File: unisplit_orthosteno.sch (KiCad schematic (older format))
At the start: 53 parts, among them U1 ProMicro

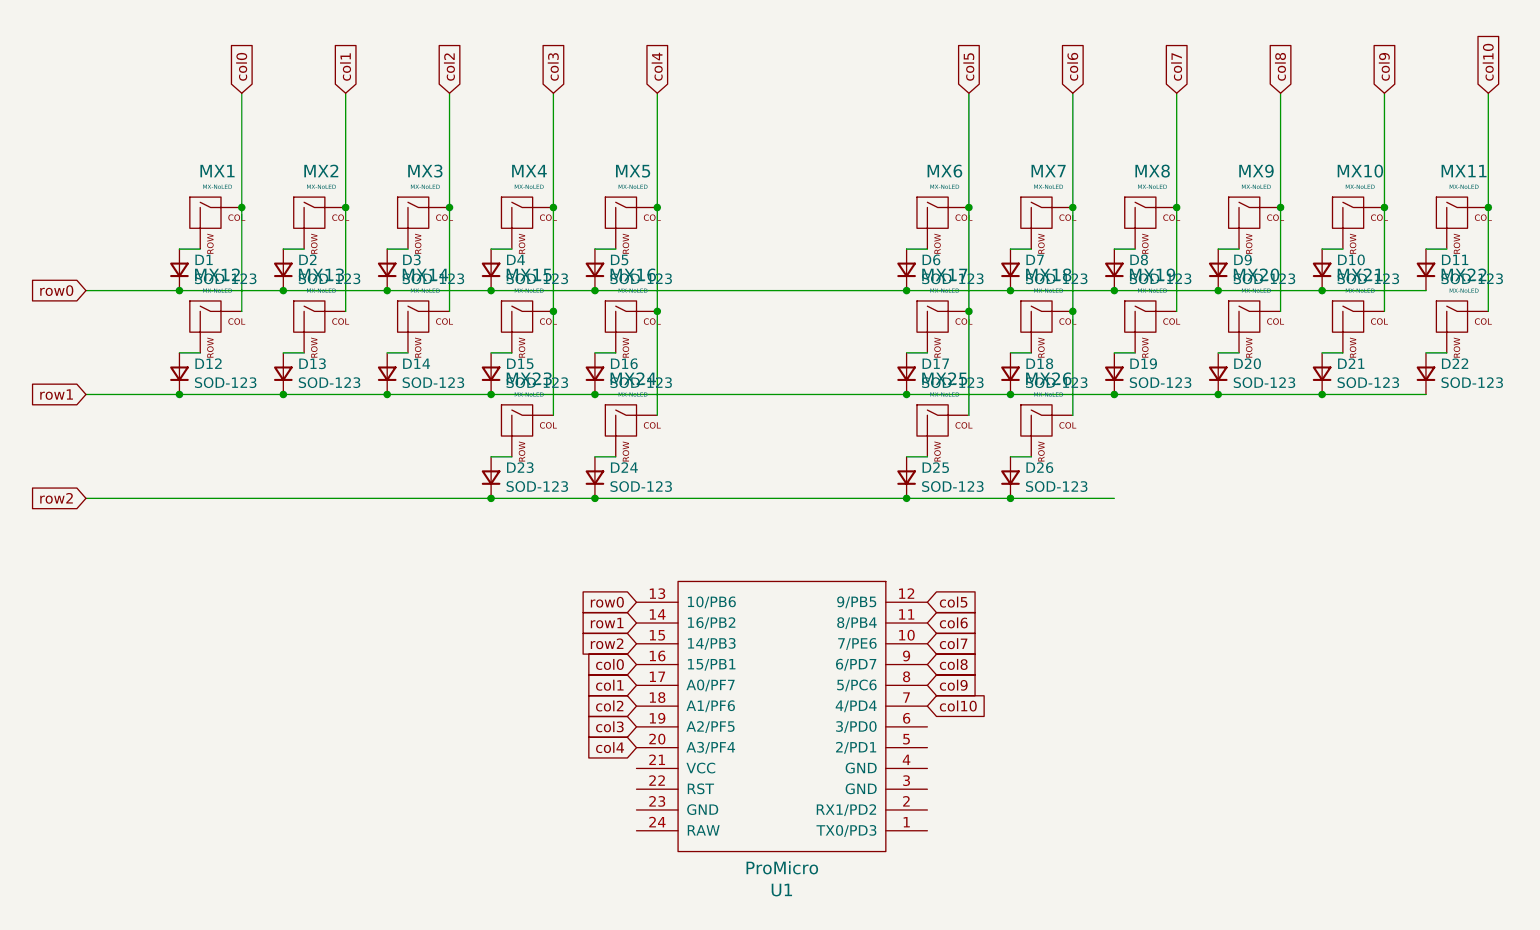
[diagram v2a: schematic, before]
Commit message: finished routing but possible problem in column 3 and 4 which I asked and reddit
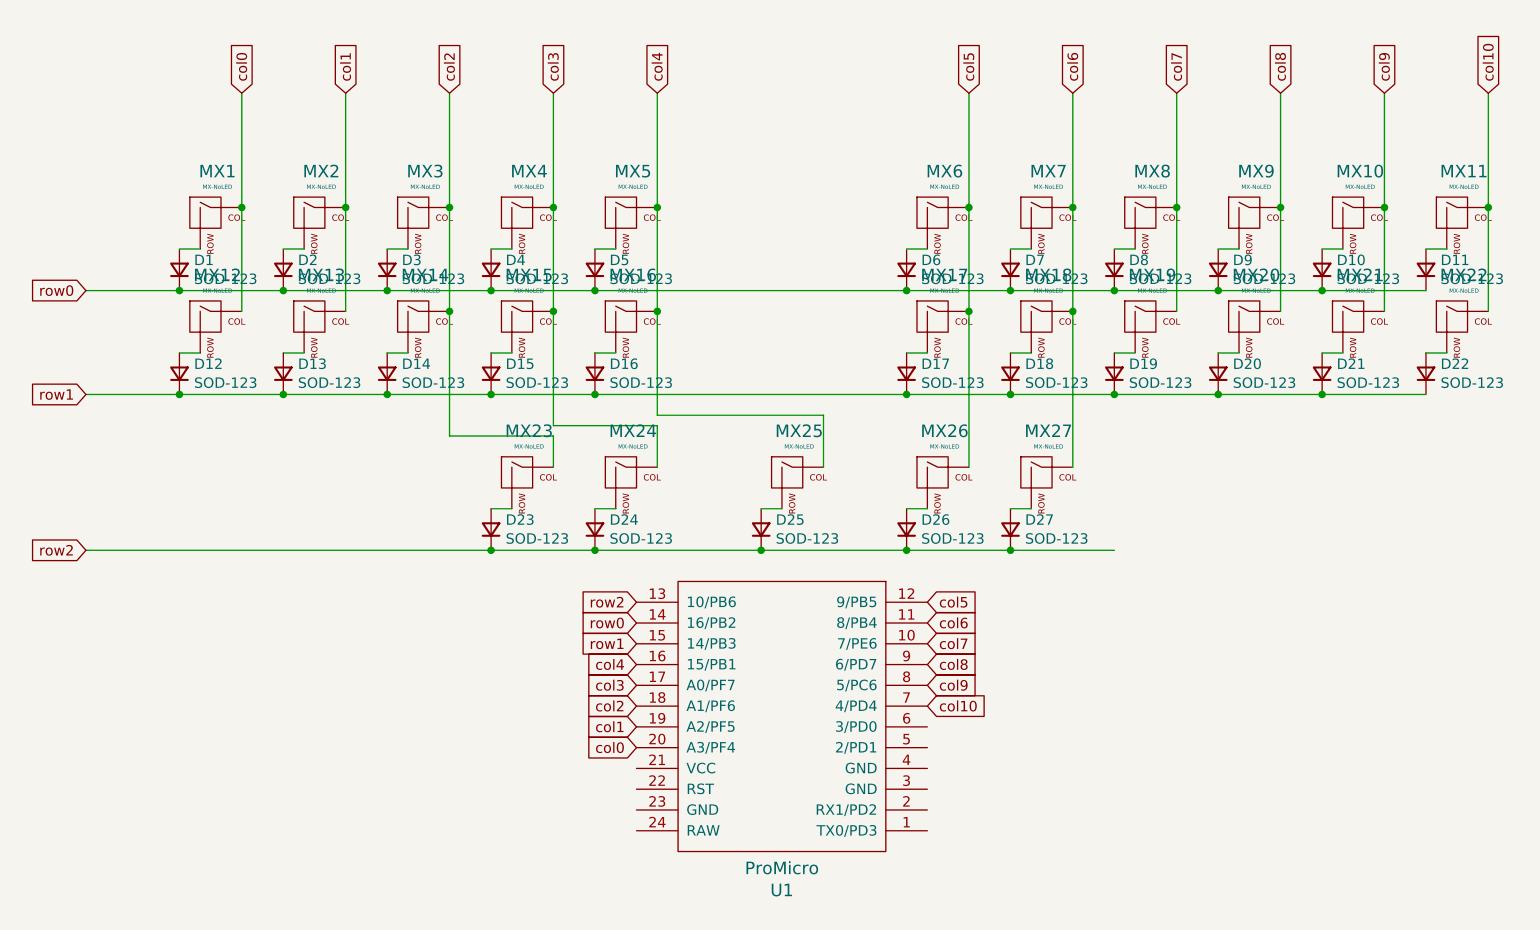
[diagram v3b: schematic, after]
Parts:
- added D25: SOD-123, Keebio-Parts:D_SOD123, symbol Device:D_Small
- added MX25: MX-NoLED, Keebio-Parts:MX-Alps-Choc-1U-NoLED, symbol MX_Alps_Hybrid:MX-NoLED
- renumbered D25 to D26, D26 to D27, MX25 to MX26, MX26 to MX27
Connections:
- net col0: now also U1.20 (A3/PF4); no longer U1.16 (15/PB1)
- net col1: now also U1.19 (A2/PF5); no longer U1.17 (A0/PF7)
- net col2: now also MX23.1 (COL)
- net col3: now also MX24.1 (COL), U1.17 (A0/PF7); no longer MX23.1 (COL), U1.19 (A2/PF5)
- net col4: now also U1.16 (15/PB1), MX25.1 (COL); no longer MX24.1 (COL), U1.20 (A3/PF4)
- net row0: now also U1.14 (16/PB2); no longer U1.13 (10/PB6)
- net row1: now also U1.15 (14/PB3); no longer U1.14 (16/PB2)
- net row2: now also U1.13 (10/PB6), D25.1 (K); no longer U1.15 (14/PB3)
- new net: D25.2 (A), MX25.2 (ROW)
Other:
- moved on the sheet: D23, D24, D26, D27, MX23, MX24, MX26, MX27
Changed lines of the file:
@@
-$Comp
-L MX_Alps_Hybrid:MX-NoLED MX?
-U 1 1 6009990C
-P 4100 3100
-AR Path="/6008E628" Ref="MX?"  Part="1"
-AR Path="/6009990C" Ref="MX23"  Part="1"
-F 0 "MX23" H 4133 3323 60  0000 C CNN
-F 1 "MX-NoLED" H 4133 3249 20  0000 C CNN
-F 2 "Keebio-Parts:MX-Alps-Choc-1U-NoLED" H 3475 3075 60  0001 C CNN
-F 3 "" H 3475 3075 60  0001 C CNN
-	1    4100 3100
-	1    0    0    -1
-$EndComp
-$Comp
-L MX_Alps_Hybrid:MX-NoLED MX24
-U 1 1 600999EE
-P 4600 3100
-F 0 "MX24" H 4633 3323 60  0000 C CNN
-F 1 "MX-NoLED" H 4633 3249 20  0000 C CNN
-F 2 "Keebio-Parts:MX-Alps-Choc-1U-NoLED" H 3975 3075 60  0001 C CNN
-F 3 "" H 3975 3075 60  0001 C CNN
-	1    4600 3100
-	1    0    0    -1
-$EndComp
 $Comp
 L MX_Alps_Hybrid:MX-NoLED MX?
@@
 $Comp
 L MX_Alps_Hybrid:MX-NoLED MX?
-U 1 1 6009A7CA
-P 6100 3100
-AR Path="/6008E628" Ref="MX?"  Part="1"
-AR Path="/6009A7CA" Ref="MX25"  Part="1"
-F 0 "MX25" H 6133 3323 60  0000 C CNN
-F 1 "MX-NoLED" H 6133 3249 20  0000 C CNN
-F 2 "Keebio-Parts:MX-Alps-Choc-1U-NoLED" H 5475 3075 60  0001 C CNN
-F 3 "" H 5475 3075 60  0001 C CNN
-	1    6100 3100
-	1    0    0    -1
-$EndComp
-$Comp
-L MX_Alps_Hybrid:MX-NoLED MX26
-U 1 1 6009A7D4
-P 6600 3100
-F 0 "MX26" H 6633 3323 60  0000 C CNN
-F 1 "MX-NoLED" H 6633 3249 20  0000 C CNN
-F 2 "Keebio-Parts:MX-Alps-Choc-1U-NoLED" H 5975 3075 60  0001 C CNN
-F 3 "" H 5975 3075 60  0001 C CNN
-	1    6600 3100
-	1    0    0    -1
-$EndComp
-$Comp
-L MX_Alps_Hybrid:MX-NoLED MX?
 U 1 1 600A326C
 P 8600 2100
@@
 	0    -1   -1   0
 $EndComp
-$Comp
-L Device:D_Small D23
-U 1 1 600BD975
-P 3950 3350
-F 0 "D23" V 3996 3280 50  0000 R CNN
-F 1 "SOD-123" V 3905 3280 50  0000 R CNN
-F 2 "Keebio-Parts:D_SOD123" V 3950 3350 50  0001 C CNN
-F 3 "~" V 3950 3350 50  0001 C CNN
-	1    3950 3350
-	0    -1   -1   0
-$EndComp
-$Comp
-L Device:D_Small D24
-U 1 1 600BE1C4
-P 4450 3350
-F 0 "D24" V 4496 3280 50  0000 R CNN
-F 1 "SOD-123" V 4405 3280 50  0000 R CNN
-F 2 "Keebio-Parts:D_SOD123" V 4450 3350 50  0001 C CNN
-F 3 "~" V 4450 3350 50  0001 C CNN
-	1    4450 3350
-	0    -1   -1   0
-$EndComp
-$Comp
-L Device:D_Small D25
-U 1 1 600BE3C9
-P 5950 3350
-F 0 "D25" V 5996 3280 50  0000 R CNN
-F 1 "SOD-123" V 5905 3280 50  0000 R CNN
-F 2 "Keebio-Parts:D_SOD123" V 5950 3350 50  0001 C CNN
-F 3 "~" V 5950 3350 50  0001 C CNN
-	1    5950 3350
-	0    -1   -1   0
-$EndComp
-$Comp
-L Device:D_Small D26
-U 1 1 600BE81C
-P 6450 3350
-F 0 "D26" V 6496 3280 50  0000 R CNN
-F 1 "SOD-123" V 6405 3280 50  0000 R CNN
-F 2 "Keebio-Parts:D_SOD123" V 6450 3350 50  0001 C CNN
-F 3 "~" V 6450 3350 50  0001 C CNN
-	1    6450 3350
-	0    -1   -1   0
-$EndComp
 Wire Wire Line
 	2450 2250 2550 2250
@@
 	4450 2750 4550 2750
 Wire Wire Line
-	3950 3250 4050 3250
-Wire Wire Line
-	4450 3250 4550 3250
-Wire Wire Line
 	5950 2250 6050 2250
 Wire Wire Line
@@
 Wire Wire Line
 	5950 2750 6050 2750
-Wire Wire Line
-	5950 3250 6050 3250
-Wire Wire Line
-	6450 3250 6550 3250
 Wire Wire Line
 	7450 2250 7550 2250
@@
 Wire Wire Line
 	7950 2950 8450 2950
-Wire Wire Line
-	6950 3450 6450 3450
-Connection ~ 3950 3450
-Connection ~ 6450 3450
-Wire Wire Line
-	6450 3450 5950 3450
 Wire Wire Line
 	2750 2550 2750 2050
@@
 Text GLabel 2000 2950 0    50   Input ~ 0
 row1
-Text GLabel 2000 3450 0    50   Input ~ 0
-row2
 Text GLabel 2750 1500 1    50   Input ~ 0
 col0
@@
 	-1   0    0    1
 $EndComp
+Text GLabel 4650 4050 0    50   Input ~ 0
+row0
+Text GLabel 4650 4150 0    50   Input ~ 0
+row1
 Text GLabel 4650 3950 0    50   Input ~ 0
-row0
-Text GLabel 4650 4050 0    50   Input ~ 0
-row1
-Text GLabel 4650 4150 0    50   Input ~ 0
 row2
-Text GLabel 4650 4250 0    50   Input ~ 0
+Text GLabel 4650 4650 0    50   Input ~ 0
 col0
-Text GLabel 4650 4350 0    50   Input ~ 0
+Text GLabel 4650 4550 0    50   Input ~ 0
 col1
 Text GLabel 4650 4450 0    50   Input ~ 0
 col2
-Text GLabel 4650 4550 0    50   Input ~ 0
-col3
-Text GLabel 4650 4650 0    50   Input ~ 0
-col4
 Text GLabel 6050 3950 2    50   Input ~ 0
 col5
@@
 Text GLabel 6050 4450 2    50   Input ~ 0
 col10
-Connection ~ 4450 3450
-Wire Wire Line
-	4450 3450 3950 3450
-Wire Wire Line
-	2000 3450 3950 3450
-Connection ~ 5950 3450
-Wire Wire Line
-	5950 3450 4450 3450
-Wire Wire Line
-	4250 2550 4250 3050
+$Comp
+L MX_Alps_Hybrid:MX-NoLED MX?
+U 1 1 6009990C
+P 4100 3350
+AR Path="/6008E628" Ref="MX?"  Part="1"
+AR Path="/6009990C" Ref="MX23"  Part="1"
+F 0 "MX23" H 4133 3573 60  0000 C CNN
+F 1 "MX-NoLED" H 4133 3499 20  0000 C CNN
+F 2 "Keebio-Parts:MX-Alps-Choc-1U-NoLED" H 3475 3325 60  0001 C CNN
+F 3 "" H 3475 3325 60  0001 C CNN
+	1    4100 3350
+	1    0    0    -1
+$EndComp
+$Comp
+L MX_Alps_Hybrid:MX-NoLED MX24
+U 1 1 600999EE
+P 4600 3350
+F 0 "MX24" H 4633 3573 60  0000 C CNN
+F 1 "MX-NoLED" H 4633 3499 20  0000 C CNN
+F 2 "Keebio-Parts:MX-Alps-Choc-1U-NoLED" H 3975 3325 60  0001 C CNN
+F 3 "" H 3975 3325 60  0001 C CNN
+	1    4600 3350
+	1    0    0    -1
+$EndComp
+$Comp
+L MX_Alps_Hybrid:MX-NoLED MX?
+U 1 1 6009A7CA
+P 6100 3350
+AR Path="/6008E628" Ref="MX?"  Part="1"
+AR Path="/6009A7CA" Ref="MX26"  Part="1"
+F 0 "MX26" H 6133 3573 60  0000 C CNN
+F 1 "MX-NoLED" H 6133 3499 20  0000 C CNN
+F 2 "Keebio-Parts:MX-Alps-Choc-1U-NoLED" H 5475 3325 60  0001 C CNN
+F 3 "" H 5475 3325 60  0001 C CNN
+	1    6100 3350
+	1    0    0    -1
+$EndComp
+$Comp
+L MX_Alps_Hybrid:MX-NoLED MX27
+U 1 1 6009A7D4
+P 6600 3350
+F 0 "MX27" H 6633 3573 60  0000 C CNN
+F 1 "MX-NoLED" H 6633 3499 20  0000 C CNN
+F 2 "Keebio-Parts:MX-Alps-Choc-1U-NoLED" H 5975 3325 60  0001 C CNN
+F 3 "" H 5975 3325 60  0001 C CNN
+	1    6600 3350
+	1    0    0    -1
+$EndComp
+$Comp
+L Device:D_Small D23
+U 1 1 600BD975
+P 3950 3600
+F 0 "D23" V 3996 3530 50  0000 R CNN
+F 1 "SOD-123" V 3905 3530 50  0000 R CNN
+F 2 "Keebio-Parts:D_SOD123" V 3950 3600 50  0001 C CNN
+F 3 "~" V 3950 3600 50  0001 C CNN
+	1    3950 3600
+	0    -1   -1   0
+$EndComp
+$Comp
+L Device:D_Small D24
+U 1 1 600BE1C4
+P 4450 3600
+F 0 "D24" V 4496 3530 50  0000 R CNN
+F 1 "SOD-123" V 4405 3530 50  0000 R CNN
+F 2 "Keebio-Parts:D_SOD123" V 4450 3600 50  0001 C CNN
+F 3 "~" V 4450 3600 50  0001 C CNN
+	1    4450 3600
+	0    -1   -1   0
+$EndComp
+$Comp
+L Device:D_Small D26
+U 1 1 600BE3C9
+P 5950 3600
+F 0 "D26" V 5996 3530 50  0000 R CNN
+F 1 "SOD-123" V 5905 3530 50  0000 R CNN
+F 2 "Keebio-Parts:D_SOD123" V 5950 3600 50  0001 C CNN
+F 3 "~" V 5950 3600 50  0001 C CNN
+	1    5950 3600
+	0    -1   -1   0
+$EndComp
+$Comp
+L Device:D_Small D27
+U 1 1 600BE81C
+P 6450 3600
+F 0 "D27" V 6496 3530 50  0000 R CNN
+F 1 "SOD-123" V 6405 3530 50  0000 R CNN
+F 2 "Keebio-Parts:D_SOD123" V 6450 3600 50  0001 C CNN
+F 3 "~" V 6450 3600 50  0001 C CNN
+	1    6450 3600
+	0    -1   -1   0
+$EndComp
+Wire Wire Line
+	3950 3500 4050 3500
+Wire Wire Line
+	4450 3500 4550 3500
+Wire Wire Line
+	5950 3500 6050 3500
+Wire Wire Line
+	6450 3500 6550 3500
+Wire Wire Line
+	6950 3700 6450 3700
+Connection ~ 3950 3700
+Connection ~ 6450 3700
+Wire Wire Line
+	6450 3700 5950 3700
+Text GLabel 2000 3700 0    50   Input ~ 0
+row2
+Connection ~ 4450 3700
+Wire Wire Line
+	4450 3700 3950 3700
+Wire Wire Line
+	2000 3700 3950 3700
+Connection ~ 5950 3700
+Wire Wire Line
+	5950 3700 5250 3700
+$Comp
+L MX_Alps_Hybrid:MX-NoLED MX?
+U 1 1 600EED95
+P 5400 3350
+AR Path="/6008E628" Ref="MX?"  Part="1"
+AR Path="/600EED95" Ref="MX25"  Part="1"
+F 0 "MX25" H 5433 3573 60  0000 C CNN
+F 1 "MX-NoLED" H 5433 3499 20  0000 C CNN
+F 2 "Keebio-Parts:MX-Alps-Choc-1U-NoLED" H 4775 3325 60  0001 C CNN
+F 3 "" H 4775 3325 60  0001 C CNN
+	1    5400 3350
+	1    0    0    -1
+$EndComp
+$Comp
+L Device:D_Small D25
+U 1 1 600EF1FB
+P 5250 3600
+F 0 "D25" V 5296 3530 50  0000 R CNN
+F 1 "SOD-123" V 5205 3530 50  0000 R CNN
+F 2 "Keebio-Parts:D_SOD123" V 5250 3600 50  0001 C CNN
+F 3 "~" V 5250 3600 50  0001 C CNN
+	1    5250 3600
+	0    -1   -1   0
+$EndComp
+Wire Wire Line
+	5250 3500 5350 3500
+Connection ~ 5250 3700
+Wire Wire Line
+	5250 3700 4450 3700
+Wire Wire Line
+	6250 3300 6250 2550
+Connection ~ 6250 2550
+Wire Wire Line
+	6750 3300 6750 2550
+Connection ~ 6750 2550
+Wire Wire Line
+	3750 2550 3750 3150
+Wire Wire Line
+	3750 3150 4250 3150
+Wire Wire Line
+	4250 3150 4250 3300
+Connection ~ 3750 2550
+Wire Wire Line
+	4250 2550 4250 3100
+Wire Wire Line
+	4250 3100 4750 3100
+Wire Wire Line
+	4750 3100 4750 3300
 Connection ~ 4250 2550
 Wire Wire Line
 	4750 2550 4750 3050
+Wire Wire Line
+	4750 3050 5550 3050
+Wire Wire Line
+	5550 3050 5550 3300
 Connection ~ 4750 2550
-Wire Wire Line
-	6250 2550 6250 3050
-Connection ~ 6250 2550
-Wire Wire Line
-	6750 3050 6750 2550
-Connection ~ 6750 2550
+Text GLabel 4650 4350 0    50   Input ~ 0
+col3
+Text GLabel 4650 4250 0    50   Input ~ 0
+col4
 $EndSCHEMATC
